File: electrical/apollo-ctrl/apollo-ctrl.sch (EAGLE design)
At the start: 65 parts, among them Q1 N-chan, Q2 N-chan, U1 NANO, U2 ADAFRUIT-MPRLS, X1 BARREL-JACK, X2 SENSOR-O2, X4 FAN

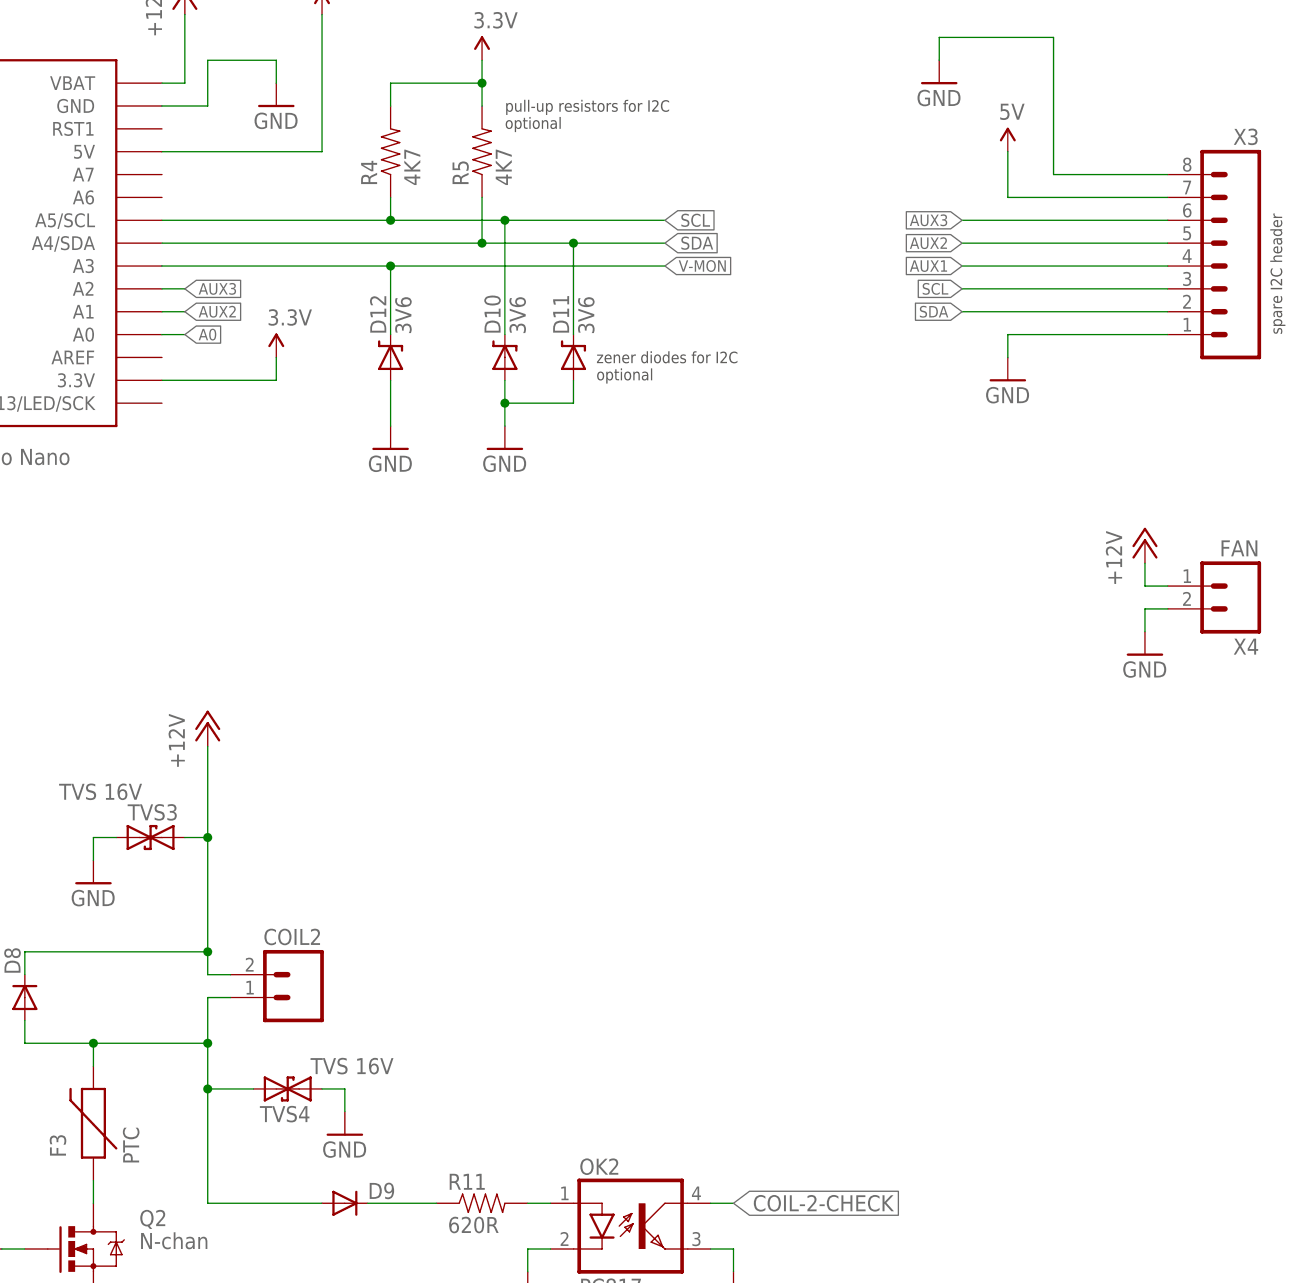
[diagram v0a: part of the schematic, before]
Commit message: ctrl pcb, more silk text, added extra ADC pins
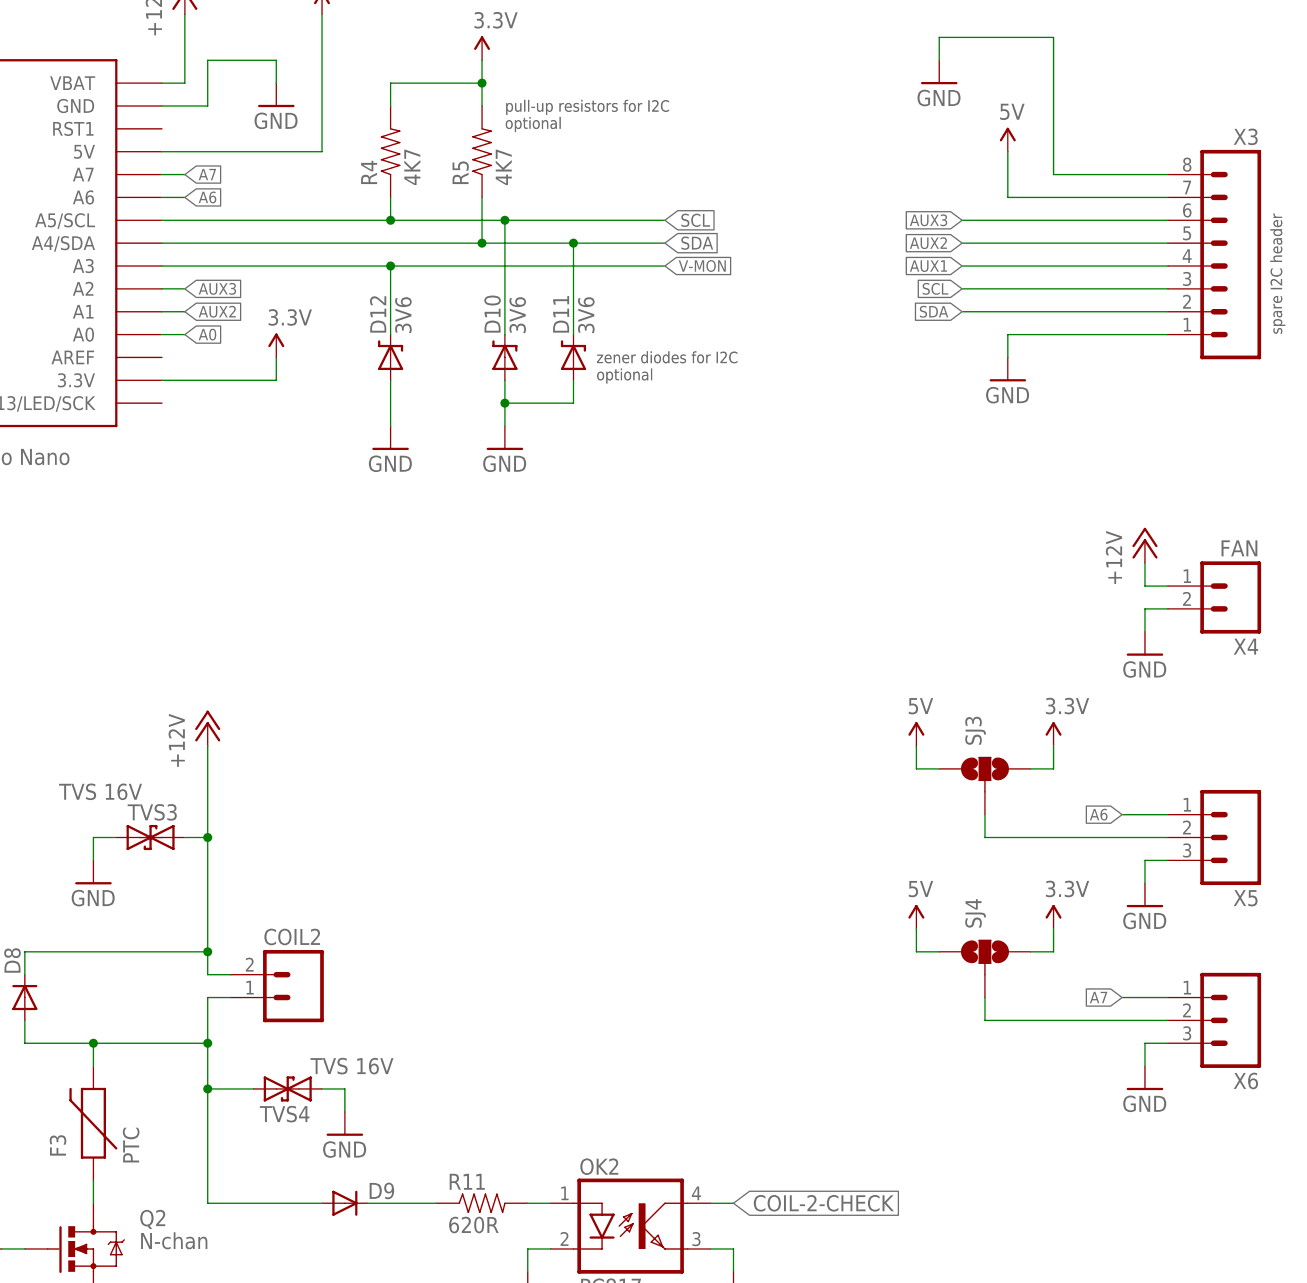
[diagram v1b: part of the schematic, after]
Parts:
- added SJ3, SJ4: (no value), apollo-ctrl:SOLDERJUMPER_2WAYS
- added X5, X6: (no value), apollo-ctrl:M03PTH
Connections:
- new net A6: U1.A6, X5.1
- new net A7: U1.A7, X6.1
- new net N$21: SJ4.2, X6.2
- new net N$22: SJ3.2, X5.2
- net 3.3V: now also SJ3.3, SJ4.3
- net 5V: now also SJ3.1, SJ4.1
- net GND: now also X5.3, X6.3
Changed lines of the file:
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@@
 <part name="SG3" library="apollo-ctrl" deviceset="M01" device="-TH-NS" value="BUZZER"/>
 <part name="SG4" library="apollo-ctrl" deviceset="M01" device="-TH-NS" value="BUZZER"/>
+<part name="X5" library="apollo-ctrl" deviceset="M03" device="PTH"/>
+<part name="GND33" library="apollo-ctrl" deviceset="GND" device=""/>
+<part name="P+13" library="apollo-ctrl" deviceset="5V" device=""/>
+<part name="X6" library="apollo-ctrl" deviceset="M03" device="PTH"/>
+<part name="GND34" library="apollo-ctrl" deviceset="GND" device=""/>
+<part name="P+14" library="apollo-ctrl" deviceset="5V" device=""/>
+<part name="P+15" library="apollo-ctrl" deviceset="3.3V" device=""/>
+<part name="SJ3" library="apollo-ctrl" deviceset="SOLDERJUMPER_2WAY" device="S"/>
+<part name="SJ4" library="apollo-ctrl" deviceset="SOLDERJUMPER_2WAY" device="S"/>
+<part name="P+16" library="apollo-ctrl" deviceset="3.3V" device=""/>
 </parts>
 <sheets>
@@
 <instance part="SG3" gate="G$1" x="-40.64" y="157.48" rot="R180"/>
 <instance part="SG4" gate="G$1" x="-40.64" y="170.18" rot="R180"/>
+<instance part="X5" gate="G$1" x="172.72" y="-25.4" rot="R180"/>
+<instance part="GND33" gate="1" x="162.56" y="-33.02" smashed="yes">
+<attribute name="VALUE" x="160.02" y="-35.56" size="1.778" layer="96"/>
+</instance>
+<instance part="P+13" gate="G$1" x="137.16" y="-15.24" smashed="yes">
+<attribute name="VALUE" x="136.144" y="-11.684" size="1.778" layer="96"/>
+</instance>
+<instance part="X6" gate="G$1" x="172.72" y="-45.72" rot="R180"/>
+<instance part="GND34" gate="1" x="162.56" y="-53.34" smashed="yes">
+<attribute name="VALUE" x="160.02" y="-55.88" size="1.778" layer="96"/>
+</instance>
+<instance part="P+14" gate="G$1" x="137.16" y="-35.56" smashed="yes">
+<attribute name="VALUE" x="136.144" y="-32.004" size="1.778" layer="96"/>
+</instance>
+<instance part="P+15" gate="G$1" x="152.4" y="-15.24"/>
+<instance part="SJ3" gate="G$1" x="144.78" y="-17.78" rot="R90"/>
+<instance part="SJ4" gate="G$1" x="144.78" y="-38.1" rot="R90"/>
+<instance part="P+16" gate="G$1" x="152.4" y="-35.56"/>
 </instances>
 <busses>
@@
 <pinref part="GND32" gate="1" pin="GND"/>
 <wire x1="162.56" y1="0" x2="162.56" y2="-2.54" width="0.1524" layer="91"/>
+</segment>
+<segment>
+<pinref part="X5" gate="G$1" pin="3"/>
+<pinref part="GND33" gate="1" pin="GND"/>
+<wire x1="165.1" y1="-27.94" x2="162.56" y2="-27.94" width="0.1524" layer="91"/>
+<wire x1="162.56" y1="-27.94" x2="162.56" y2="-30.48" width="0.1524" layer="91"/>
+</segment>
+<segment>
+<pinref part="X6" gate="G$1" pin="3"/>
+<pinref part="GND34" gate="1" pin="GND"/>
+<wire x1="165.1" y1="-48.26" x2="162.56" y2="-48.26" width="0.1524" layer="91"/>
+<wire x1="162.56" y1="-48.26" x2="162.56" y2="-50.8" width="0.1524" layer="91"/>
 </segment>
 </net>
@@
 <wire x1="81.28" y1="139.7" x2="81.28" y2="142.24" width="0.1524" layer="91"/>
 </segment>
+<segment>
+<pinref part="SJ4" gate="G$1" pin="1"/>
+<pinref part="P+14" gate="G$1" pin="5V"/>
+<wire x1="139.7" y1="-38.1" x2="137.16" y2="-38.1" width="0.1524" layer="91"/>
+<wire x1="137.16" y1="-38.1" x2="137.16" y2="-35.56" width="0.1524" layer="91"/>
+</segment>
+<segment>
+<pinref part="SJ3" gate="G$1" pin="1"/>
+<pinref part="P+13" gate="G$1" pin="5V"/>
+<wire x1="139.7" y1="-17.78" x2="137.16" y2="-17.78" width="0.1524" layer="91"/>
+<wire x1="137.16" y1="-17.78" x2="137.16" y2="-15.24" width="0.1524" layer="91"/>
+</segment>
 </net>
 <net name="COIL-2-CHECK" class="0">
@@
 <pinref part="P+5" gate="G$1" pin="3.3V"/>
 </segment>
+<segment>
+<pinref part="P+15" gate="G$1" pin="3.3V"/>
+<wire x1="152.4" y1="-15.24" x2="152.4" y2="-17.78" width="0.1524" layer="91"/>
+<pinref part="SJ3" gate="G$1" pin="3"/>
+<wire x1="152.4" y1="-17.78" x2="149.86" y2="-17.78" width="0.1524" layer="91"/>
+</segment>
+<segment>
+<pinref part="P+16" gate="G$1" pin="3.3V"/>
+<wire x1="152.4" y1="-35.56" x2="152.4" y2="-38.1" width="0.1524" layer="91"/>
+<pinref part="SJ4" gate="G$1" pin="3"/>
+<wire x1="152.4" y1="-38.1" x2="149.86" y2="-38.1" width="0.1524" layer="91"/>
+</segment>
 </net>
 <net name="BUTTON" class="0">
@@
 </segment>
 </net>
+<net name="A6" class="0">
+<segment>
+<pinref part="X5" gate="G$1" pin="1"/>
+<wire x1="165.1" y1="-22.86" x2="160.02" y2="-22.86" width="0.1524" layer="91"/>
+<label x="160.02" y="-22.86" size="1.27" layer="95" rot="R180" xref="yes"/>
+</segment>
+<segment>
+<pinref part="U1" gate="G$1" pin="A6"/>
+<wire x1="53.34" y1="45.72" x2="55.88" y2="45.72" width="0.1524" layer="91"/>
+<label x="55.88" y="45.72" size="1.27" layer="95" xref="yes"/>
+</segment>
+</net>
+<net name="A7" class="0">
+<segment>
+<pinref part="X6" gate="G$1" pin="1"/>
+<wire x1="165.1" y1="-43.18" x2="160.02" y2="-43.18" width="0.1524" layer="91"/>
+<label x="160.02" y="-43.18" size="1.27" layer="95" rot="R180" xref="yes"/>
+</segment>
+<segment>
+<pinref part="U1" gate="G$1" pin="A7"/>
+<wire x1="53.34" y1="48.26" x2="55.88" y2="48.26" width="0.1524" layer="91"/>
+<label x="55.88" y="48.26" size="1.27" layer="95" xref="yes"/>
+</segment>
+</net>
+<net name="N$21" class="0">
+<segment>
+<pinref part="X6" gate="G$1" pin="2"/>
+<pinref part="SJ4" gate="G$1" pin="2"/>
+<wire x1="165.1" y1="-45.72" x2="144.78" y2="-45.72" width="0.1524" layer="91"/>
+<wire x1="144.78" y1="-45.72" x2="144.78" y2="-43.18" width="0.1524" layer="91"/>
+</segment>
+</net>
+<net name="N$22" class="0">
+<segment>
+<pinref part="X5" gate="G$1" pin="2"/>
+<pinref part="SJ3" gate="G$1" pin="2"/>
+<wire x1="165.1" y1="-25.4" x2="144.78" y2="-25.4" width="0.1524" layer="91"/>
+<wire x1="144.78" y1="-25.4" x2="144.78" y2="-22.86" width="0.1524" layer="91"/>
+</segment>
+</net>
